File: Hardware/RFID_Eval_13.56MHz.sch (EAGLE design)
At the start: 36 parts, among them U1 DNP_SM130, U3 ARDUINO_SHIELDNOLABELS

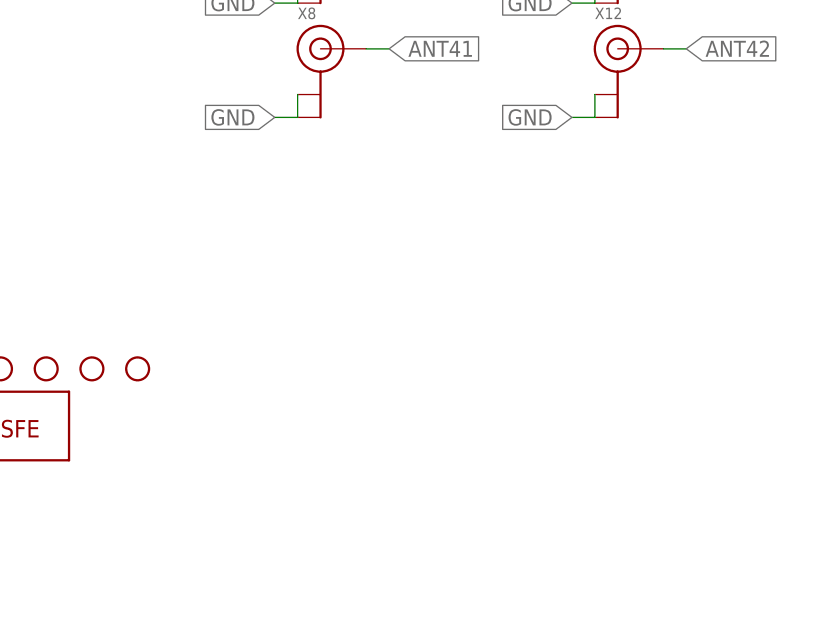
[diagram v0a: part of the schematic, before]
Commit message: Added 3 more u.FL connectors for testing purpose
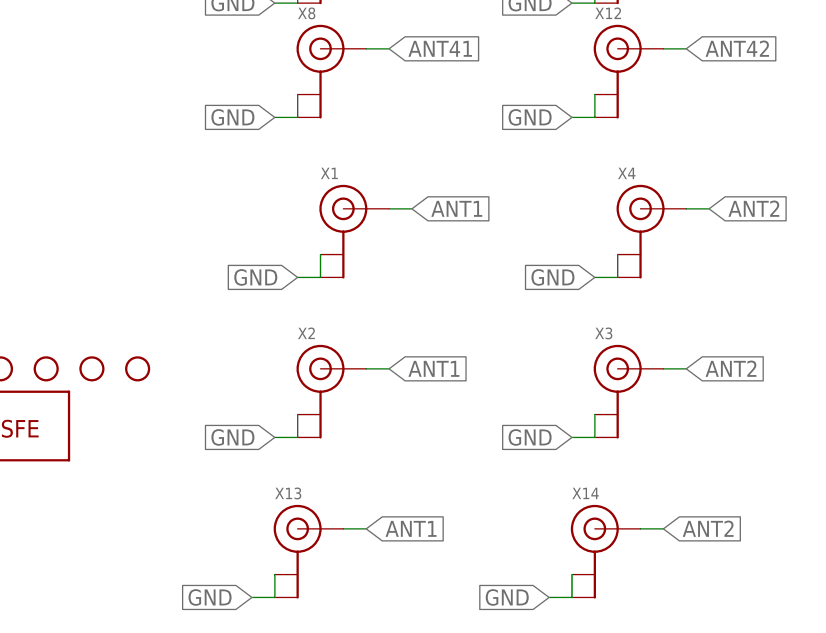
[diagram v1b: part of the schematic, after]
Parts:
- added X1, X13, X14, X2, X3, X4: (no value), adafruit:ANTENNA_U.FL
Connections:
- net ANT1: now also X1.SIGNAL, X13.SIGNAL, X2.SIGNAL
- net ANT2: now also X14.SIGNAL, X3.SIGNAL, X4.SIGNAL
- net GND: now also X1.GND@0, X1.GND@1, X13.GND@0, X13.GND@1, X14.GND@0, X14.GND@1, X2.GND@0, X2.GND@1, X3.GND@0, X3.GND@1, X4.GND@0, X4.GND@1
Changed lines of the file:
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@@
 <part name="X11" library="adafruit" deviceset="ANTENNA_U.FL" device=""/>
 <part name="X12" library="adafruit" deviceset="ANTENNA_U.FL" device=""/>
+<part name="X1" library="adafruit" deviceset="ANTENNA_U.FL" device=""/>
+<part name="X4" library="adafruit" deviceset="ANTENNA_U.FL" device=""/>
+<part name="X2" library="adafruit" deviceset="ANTENNA_U.FL" device=""/>
+<part name="X3" library="adafruit" deviceset="ANTENNA_U.FL" device=""/>
+<part name="X13" library="adafruit" deviceset="ANTENNA_U.FL" device=""/>
+<part name="X14" library="adafruit" deviceset="ANTENNA_U.FL" device=""/>
 </parts>
 <sheets>
@@
 <instance part="X11" gate="G$1" x="299.72" y="81.28"/>
 <instance part="X12" gate="G$1" x="299.72" y="68.58"/>
+<instance part="X1" gate="G$1" x="269.24" y="50.8"/>
+<instance part="X4" gate="G$1" x="302.26" y="50.8"/>
+<instance part="X2" gate="G$1" x="266.7" y="33.02"/>
+<instance part="X3" gate="G$1" x="299.72" y="33.02"/>
+<instance part="X13" gate="G$1" x="264.16" y="15.24"/>
+<instance part="X14" gate="G$1" x="297.18" y="15.24"/>
 </instances>
 <busses>
@@
 <label x="294.64" y="60.96" size="1.778" layer="95" rot="R180" xref="yes"/>
 </segment>
+<segment>
+<pinref part="X1" gate="G$1" pin="GND@0"/>
+<pinref part="X1" gate="G$1" pin="GND@1"/>
+<wire x1="266.7" y1="45.72" x2="266.7" y2="43.18" width="0.1524" layer="91"/>
+<wire x1="266.7" y1="43.18" x2="264.16" y2="43.18" width="0.1524" layer="91"/>
+<label x="264.16" y="43.18" size="1.778" layer="95" rot="R180" xref="yes"/>
+</segment>
+<segment>
+<pinref part="X4" gate="G$1" pin="GND@0"/>
+<pinref part="X4" gate="G$1" pin="GND@1"/>
+<wire x1="299.72" y1="45.72" x2="299.72" y2="43.18" width="0.1524" layer="91"/>
+<wire x1="299.72" y1="43.18" x2="297.18" y2="43.18" width="0.1524" layer="91"/>
+<label x="297.18" y="43.18" size="1.778" layer="95" rot="R180" xref="yes"/>
+</segment>
+<segment>
+<pinref part="X2" gate="G$1" pin="GND@0"/>
+<pinref part="X2" gate="G$1" pin="GND@1"/>
+<wire x1="264.16" y1="27.94" x2="264.16" y2="25.4" width="0.1524" layer="91"/>
+<wire x1="264.16" y1="25.4" x2="261.62" y2="25.4" width="0.1524" layer="91"/>
+<label x="261.62" y="25.4" size="1.778" layer="95" rot="R180" xref="yes"/>
+</segment>
+<segment>
+<pinref part="X3" gate="G$1" pin="GND@0"/>
+<pinref part="X3" gate="G$1" pin="GND@1"/>
+<wire x1="297.18" y1="27.94" x2="297.18" y2="25.4" width="0.1524" layer="91"/>
+<wire x1="297.18" y1="25.4" x2="294.64" y2="25.4" width="0.1524" layer="91"/>
+<label x="294.64" y="25.4" size="1.778" layer="95" rot="R180" xref="yes"/>
+</segment>
+<segment>
+<pinref part="X13" gate="G$1" pin="GND@0"/>
+<pinref part="X13" gate="G$1" pin="GND@1"/>
+<wire x1="261.62" y1="10.16" x2="261.62" y2="7.62" width="0.1524" layer="91"/>
+<wire x1="261.62" y1="7.62" x2="259.08" y2="7.62" width="0.1524" layer="91"/>
+<label x="259.08" y="7.62" size="1.778" layer="95" rot="R180" xref="yes"/>
+</segment>
+<segment>
+<pinref part="X14" gate="G$1" pin="GND@0"/>
+<pinref part="X14" gate="G$1" pin="GND@1"/>
+<wire x1="294.64" y1="10.16" x2="294.64" y2="7.62" width="0.1524" layer="91"/>
+<wire x1="294.64" y1="7.62" x2="292.1" y2="7.62" width="0.1524" layer="91"/>
+<label x="292.1" y="7.62" size="1.778" layer="95" rot="R180" xref="yes"/>
+</segment>
 </net>
 <net name="5V" class="0">
@@
 <label x="236.22" y="157.48" size="1.27" layer="95" xref="yes"/>
 </segment>
+<segment>
+<pinref part="X1" gate="G$1" pin="SIGNAL"/>
+<wire x1="274.32" y1="50.8" x2="276.86" y2="50.8" width="0.1524" layer="91"/>
+<label x="276.86" y="50.8" size="1.778" layer="95" xref="yes"/>
+</segment>
+<segment>
+<pinref part="X2" gate="G$1" pin="SIGNAL"/>
+<wire x1="271.78" y1="33.02" x2="274.32" y2="33.02" width="0.1524" layer="91"/>
+<label x="274.32" y="33.02" size="1.778" layer="95" xref="yes"/>
+</segment>
+<segment>
+<pinref part="X13" gate="G$1" pin="SIGNAL"/>
+<wire x1="269.24" y1="15.24" x2="271.78" y2="15.24" width="0.1524" layer="91"/>
+<label x="271.78" y="15.24" size="1.778" layer="95" xref="yes"/>
+</segment>
 </net>
 <net name="ANT2" class="0">
@@
 <label x="195.58" y="83.82" size="1.27" layer="95" xref="yes"/>
 </segment>
-</net>
+<segment>
+<pinref part="X4" gate="G$1" pin="SIGNAL"/>
+<wire x1="307.34" y1="50.8" x2="309.88" y2="50.8" width="0.1524" layer="91"/>
+<label x="309.88" y="50.8" size="1.778" layer="95" xref="yes"/>
+</segment>
+<segment>
+<pinref part="X3" gate="G$1" pin="SIGNAL"/>
+<wire x1="304.8" y1="33.02" x2="307.34" y2="33.02" width="0.1524" layer="91"/>
+<label x="307.34" y="33.02" size="1.778" layer="95" xref="yes"/>
+</segment>
+<segment>
+<pinref part="X14" gate="G$1" pin="SIGNAL"/>
+<wire x1="302.26" y1="15.24" x2="304.8" y2="15.24" width="0.1524" layer="91"/>
+<label x="304.8" y="15.24" size="1.778" layer="95" xref="yes"/>
+</segment>
+</net>
